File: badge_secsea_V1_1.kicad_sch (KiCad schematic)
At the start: 132 parts, among them J1 USB_C_Receptacle_USB2.0_14P, J2 PM254-2-06-S-8.5, J3 PM254-2-06-S-8.5, J4 AFC07-S24ECA-00, J5 Micro_SD_Card_Det1, Q1 2N7002, Q2 SI1308EDL, Q3 SI2301, SW1 TS-1187A-B-A-B, SW2 K2-1112SW-A4SW-04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

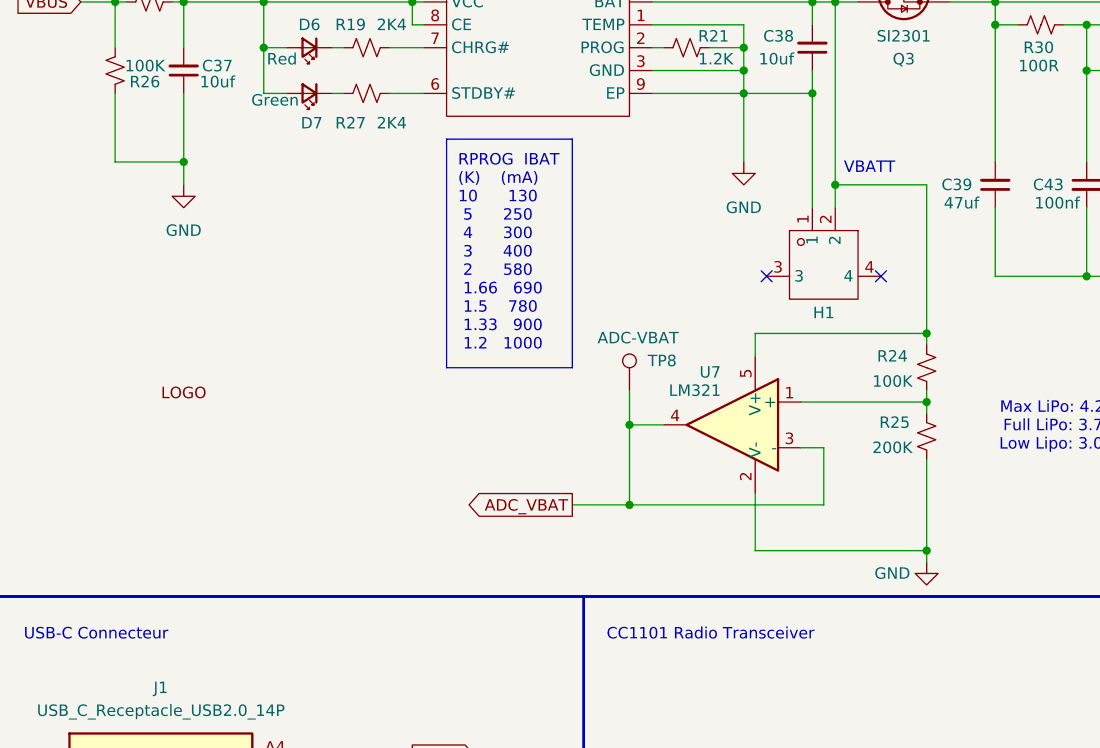
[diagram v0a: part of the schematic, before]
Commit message: Consumption fix: Op amp now connected to +3.3V instead of VBat (Schematic + PCB)
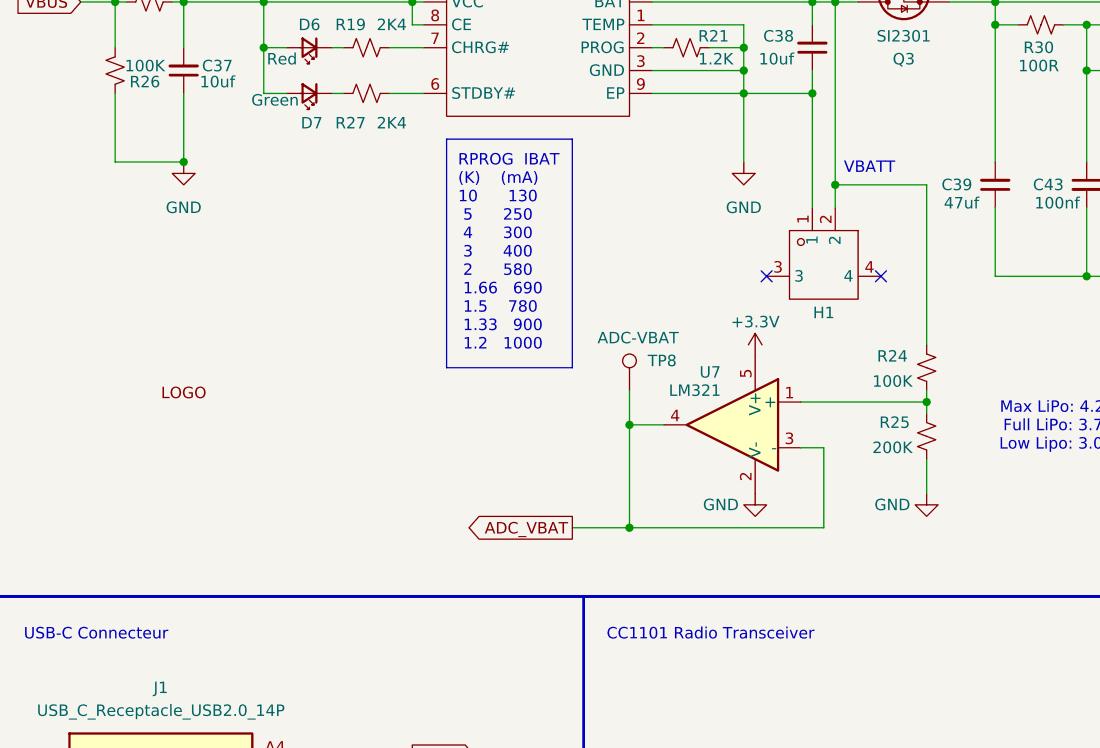
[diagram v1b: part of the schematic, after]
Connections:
- net +3.3V: now also U7.5 (V+)
- net at C38.2, H1.2, Q3.3 (D)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: no longer U7.5 (V+)

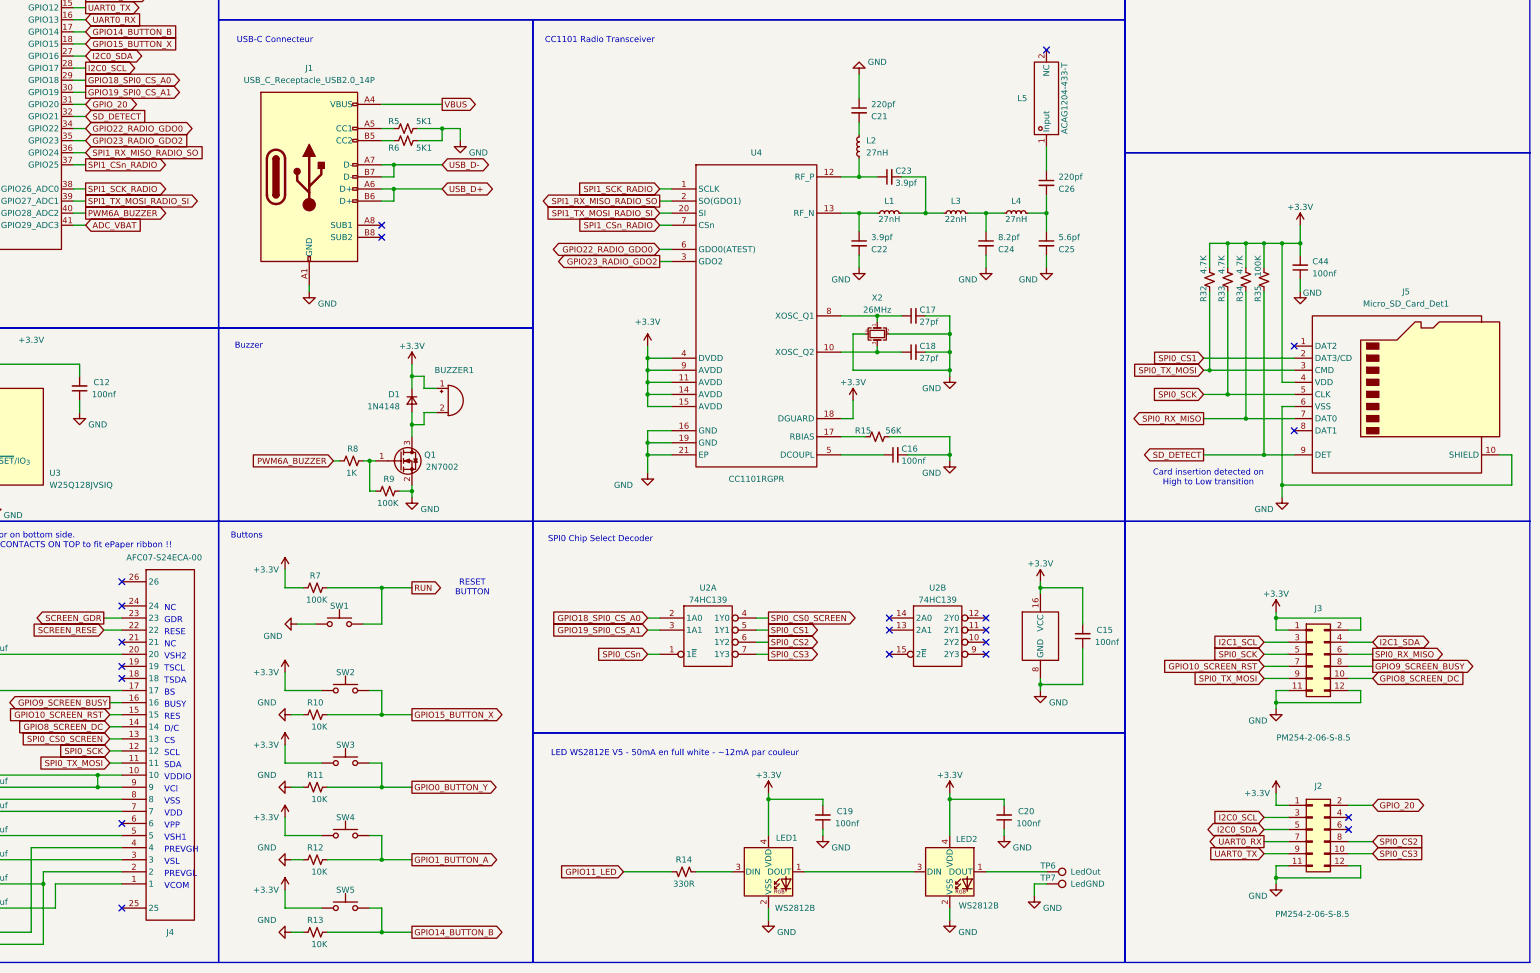
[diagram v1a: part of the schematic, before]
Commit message: SAO connector added (with 3D). WIP on the antenna.
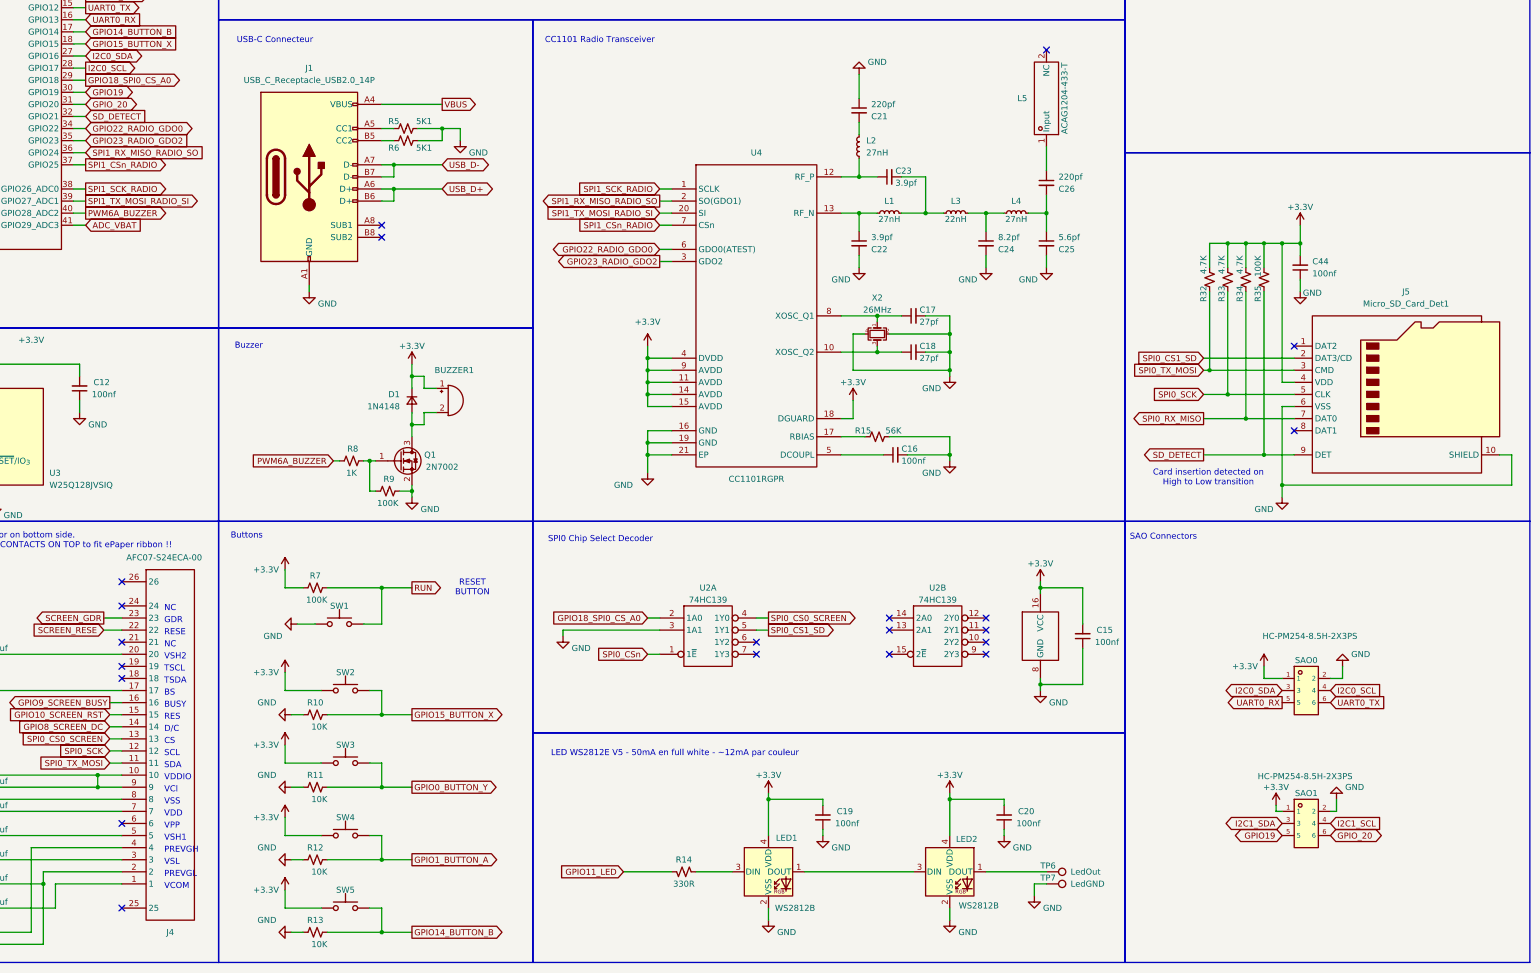
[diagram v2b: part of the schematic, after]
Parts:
- removed J2, J3: PM254-2-06-S-8.5, Connector_PinSocket_2.54mm:PinSocket_2x06_P2.54mm_Vertical_SMD, symbol Connector_Generic:Conn_02x06_Odd_Even
- added SAO0, SAO1: HC-PM254-8.5H-2X3PS, lcsc_footprints:C22373944_HDR-SMD_6P-P2_54-V-F-R2-C3-LS7_1, symbol lcsc_imported:HC-PM254-8_5H-2X3PS
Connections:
- net +3.3V: now also SAO0.1, SAO1.1
- net GND: now also U2.3 (1A1), SAO0.2, SAO1.2
- net GPIO_20: now also SAO1.6
- net I2C0_SCL: now also SAO0.4
- net I2C0_SDA: now also SAO0.3
- net I2C1_SCL: now also SAO1.4
- net I2C1_SDA: now also SAO1.3
- net UART0_RX: now also SAO0.5
- net UART0_TX: now also SAO0.6
- net GPIO19_SPI0_CS_A1 renamed GPIO19
- net GPIO19: now also SAO1.5; no longer U2.3 (1A1)
- net SPI0_CS1 renamed SPI0_CS1_SD
- net SPI0_CS2: no longer names the net of U2.6 (1Y2)
- net SPI0_CS3: no longer names the net of U2.7 (1Y3)
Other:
- note added: "SAO Connectors"

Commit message: WIP routing
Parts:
- renumbered L5 to ANT0
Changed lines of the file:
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@@
 		(in_pos_files yes)
 		(dnp no)
-		(property "Reference" "L5"
+		(property "Reference" "ANT0"
 			(at 350.52 153.67 90)
 			(show_name no)
@@
 			(project "badge_secsea_V1_1"
 				(path "/7540cf5d-38f8-4890-995a-94ee8b2f9fbe"
-					(reference "L5")
+					(reference "ANT0")
 					(unit 1)
 				)

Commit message: WIP Routing....
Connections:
- net GPIO19: now also SAO0.5; no longer SAO1.5
- net GPIO_20: now also SAO0.6; no longer SAO1.6
- net UART0_RX: now also SAO1.5; no longer SAO0.5
- net UART0_TX: now also SAO1.6; no longer SAO0.6
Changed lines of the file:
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@@
 	(global_label "UART0_RX"
 		(shape output)
-		(at 405.13 280.67 180)
-		(effects
-			(font
-				(size 1.27 1.27)
-			)
-			(justify right)
-		)
-		(property "Intersheetrefs" "${INTERSHEET_REFS}"
-			(at 405.13 280.67 0)
+		(at 405.13 308.61 180)
+		(effects
+			(font
+				(size 1.27 1.27)
+			)
+			(justify right)
+		)
+		(property "Intersheetrefs" "${INTERSHEET_REFS}"
+			(at 405.13 308.61 0)
 			(hide yes)
 			(show_name no)
@@
 	(global_label "GPIO19"
 		(shape bidirectional)
-		(at 405.13 308.61 180)
-		(effects
-			(font
-				(size 1.27 1.27)
-			)
-			(justify right)
-		)
-		(property "Intersheetrefs" "${INTERSHEET_REFS}"
-			(at 405.13 308.61 0)
+		(at 405.13 280.67 180)
+		(effects
+			(font
+				(size 1.27 1.27)
+			)
+			(justify right)
+		)
+		(property "Intersheetrefs" "${INTERSHEET_REFS}"
+			(at 405.13 280.67 0)
 			(hide yes)
 			(show_name no)
@@
 	(global_label "GPIO_20"
 		(shape bidirectional)
-		(at 415.29 308.61 0)
-		(effects
-			(font
-				(size 1.27 1.27)
-			)
-			(justify left)
-		)
-		(property "Intersheetrefs" "${INTERSHEET_REFS}"
-			(at 415.29 308.61 0)
+		(at 415.29 280.67 0)
+		(effects
+			(font
+				(size 1.27 1.27)
+			)
+			(justify left)
+		)
+		(property "Intersheetrefs" "${INTERSHEET_REFS}"
+			(at 415.29 280.67 0)
 			(hide yes)
 			(show_name no)
@@
 	(global_label "UART0_TX"
 		(shape input)
-		(at 415.29 280.67 0)
-		(effects
-			(font
-				(size 1.27 1.27)
-			)
-			(justify left)
-		)
-		(property "Intersheetrefs" "${INTERSHEET_REFS}"
-			(at 415.29 280.67 0)
-			(hide yes)
-			(show_name no)
+		(at 415.29 308.61 0)
+		(effects
+			(font
+				(size 1.27 1.27)
+			)
+			(justify left)
+		)
+		(property "Intersheetrefs" "${INTERSHEET_REFS}"
+			(at 415.29 308.61 0)
+			(hide yes)
+			(show_name no)
